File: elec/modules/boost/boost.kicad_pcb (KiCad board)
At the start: 2 copper layers, 40.6 x 61 mm, 9 parts, among them J1 Conn_01x05, J2 Conn_01x05, U1 LM2587S-ADJ

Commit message: sleepy but did most pcbs
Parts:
- added C35: 0.1uF, Capacitor_SMD:C_0603_1608Metric, F.Cu at (128.3, 102.9)
- added C36: 100uF, Capacitor_THT:CP_Radial_D8.0mm_P3.50mm, F.Cu at (130.0, 97.6)
- J1, J2: value Conn_01x05 -> Conn_01x08; footprint Pinheaders:PinHeader_1x05_P2.54mm_Vertical -> Pinheaders:PinHeader_1x08_P2.54mm_Vertical
- moved C40 36.5 mm to (149.0, 117.9), turned to 90 degrees
- moved R35 34.2 mm to (146.3, 116.9), turned to 180 degrees
- moved R38 33.9 mm to (146.3, 118.7), turned to 0 degrees
- moved J1 33.5 mm to (130.3, 91.1), turned to 90 degrees
- moved D2 32.3 mm to (149.8, 113.4), turned to 90 degrees
- moved R36 30.7 mm to (145.5, 114.4), turned to 90 degrees
- moved U1 24.6 mm to (131.5, 115.2), turned to 180 degrees
- moved J2 10.3 mm to (130.3, 123.4), turned to 90 degrees
- moved L33 9.96 mm to (138.0, 102.1), turned to 0 degrees
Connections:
- J1 pad 1: +24V -> +12V
- J1 pad 2: +24V -> +12V
- J1 pad 3: GND -> +12V
- J1 pad 4: +12V -> unconnected-(J1-Pin_4-Pad4)
- J1 pad 5: +12V -> unconnected-(J1-Pin_5-Pad5)
- J2 pad 1: +24V -> unconnected-(J2-Pin_1-Pad1)
- J2 pad 2: +24V -> unconnected-(J2-Pin_2-Pad2)
- J2 pad 3: GND -> +24V
- J2 pad 4: +12V -> +24V
- J2 pad 5: +12V -> +24V
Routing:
- net GND: vias 929 -> 2
- net +24V: vias 64 -> 0
- removed copper zone on B.Cu, net +24V
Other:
- board size 40.6 x 61 mm -> 30.5 x 40.6 mm

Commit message: finished pcbs-silkscrfeen pcbs seem halal
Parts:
- moved J1 2.49 mm to (130.3, 88.7)
- moved J2 0.20 mm to (130.3, 123.6)
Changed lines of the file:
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@@
 	(footprint "Pinheaders:PinHeader_1x08_P2.54mm_Vertical"
 		(layer "F.Cu")
-		(at 130.285 123.39 90)
+		(at 130.285 123.59 90)
 		(descr "Through hole straight pin header, 1x08, 2.54mm pitch, single row")
 		(tags "Through hole pin header THT 1x08 2.54mm single row")
@@
 	(footprint "Pinheaders:PinHeader_1x08_P2.54mm_Vertical"
 		(layer "F.Cu")
-		(at 130.285 91.14 90)
+		(at 130.285 88.65 90)
 		(descr "Through hole straight pin header, 1x08, 2.54mm pitch, single row")
 		(tags "Through hole pin header THT 1x08 2.54mm single row")
@@
 		(polygon
 			(pts
-				(xy 144.27 112.64) (xy 144.27 107.39) (xy 136.52 107.39) (xy 137.02 107.39) (xy 137.02 89.39) (xy 128.52 89.39)
+				(xy 144.27 112.64) (xy 144.27 107.39) (xy 136.52 107.39) (xy 137.02 107.39) (xy 137.02 87.14) (xy 128.52 87.14)
 				(xy 128.52 109.39) (xy 138.27 109.39) (xy 138.52 109.64) (xy 138.52 112.64)
 			)

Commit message: added silkscreen
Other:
- board text added: "design of 2-Chairs. 2025 JLC Order No. JLCJLCJLCJLC"
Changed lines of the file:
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@@
 		(layer "Edge.Cuts")
+	)
+	(gr_text "design of 2-Chairs. 2025\nJLC Order No. JLCJLCJLCJLC"
+		(at 138.77 103.14 0)
+		(layer "B.SilkS")
+		(effects
+			(font
+				(size 1 1)
+				(thickness 0.2)
+			)
+			(justify mirror)
+		)
 	)
 	(via

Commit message: did pcba for buck and boos5t
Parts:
- moved L33 6.56 mm to (144.3, 100.1)
- moved C35 5.27 mm to (132.8, 105.6)
- moved C36 4.51 mm to (134.4, 98.6)
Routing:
- net GND: vias 2 -> 3
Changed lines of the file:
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@@
 		(sheetname "/")
 		(sheetfile "boost.kicad_sch")
-		(attr through_hole)
+		(attr through_hole exclude_from_pos_files exclude_from_bom)
 		(fp_line
 			(start -1.33 -1.33)
@@
 		(sheetname "/")
 		(sheetfile "boost.kicad_sch")
-		(attr through_hole)
+		(attr through_hole exclude_from_pos_files exclude_from_bom)
 		(fp_line
 			(start 7.65 -3.26)
@@
 		(sheetname "/")
 		(sheetfile "boost.kicad_sch")
-		(attr through_hole)
+		(attr through_hole exclude_from_pos_files exclude_from_bom)
 		(fp_line
 			(start -1.33 -1.33)
@@
 	(footprint "Capacitor_THT:CP_Radial_D8.0mm_P3.50mm"
 		(layer "F.Cu")
-		(at 130.02 97.64 180)
+		(at 134.422651 98.64 180)
 		(descr "CP, Radial series, Radial, pin pitch=3.50mm, diameter=8mm, height=12mm, Electrolytic Capacitor")
 		(tags "CP Radial series Radial pin pitch 3.50mm diameter 8mm height 12mm Electrolytic Capacitor")
@@
 		(sheetname "/")
 		(sheetfile "boost.kicad_sch")
-		(attr through_hole)
+		(attr through_hole exclude_from_pos_files exclude_from_bom)
 		(fp_line
 			(start 5.83 -0.533)
@@
 	(footprint "Capacitor_SMD:C_0603_1608Metric"
 		(layer "F.Cu")
-		(at 128.27 102.89 180)
+		(at 132.77 105.64 180)
 		(descr "Capacitor SMD 0603 (1608 Metric), square (rectangular) end terminal, IPC-7351 nominal, (Body size source: IPC-SM-782 page 76, https://www.pcb-3d.com/wordpress/wp-content/uploads/ipc-sm-782a_amendment_1_and_2.pdf), generated with kicad-footprint-generator")
 		(tags "capacitor")
@@
 	(footprint "Inductor_SMD:L_APV_APH1040"
 		(layer "F.Cu")
-		(at 138.02 102.14)
+		(at 144.27 100.14)
 		(descr "Inductor, APV, APH1040, 10.8x10.0x3.8mm, (http://en.apvind.com/public/upload/20240408/996aafa961154ed753e4983e7eb80fa7.pdf), generated with kicad-footprint-generator gen_inductor.py")
 		(tags "molded power shielded")
@@
 		(net 2)
 	)
+	(via
+		(at 131.995 105.64)
+		(size 0.6)
+		(drill 0.3)
+		(layers "F.Cu" "B.Cu")
+		(net 2)
+	)
 	(zone
 		(net 5)
@@
 		(polygon
 			(pts
-				(xy 144.27 112.64) (xy 144.27 107.39) (xy 136.52 107.39) (xy 137.02 107.39) (xy 137.02 87.14) (xy 128.52 87.14)
-				(xy 128.52 109.39) (xy 138.27 109.39) (xy 138.52 109.64) (xy 138.52 112.64)
+				(xy 144.27 112.64) (xy 144.27 107.39) (xy 144.27 97.14) (xy 136.77 97.14) (xy 136.77 87.14) (xy 128.02 87.14)
+				(xy 128.02 109.39) (xy 138.27 109.39) (xy 138.52 109.64) (xy 138.52 112.64)
 			)
 		)
@@
 		(polygon
 			(pts
-				(xy 144.27 112.64) (xy 144.27 107.39) (xy 137.02 107.39) (xy 137.02 97.14) (xy 151.77 97.14) (xy 151.77 110.85)
-				(xy 146.52 110.85) (xy 146.52 112.89) (xy 144.77 112.89) (xy 144.77 114.64) (xy 140.02 114.64) (xy 140.02 112.64)
+				(xy 144.27 112.64) (xy 144.27 97.14) (xy 151.77 97.14) (xy 151.77 110.85) (xy 146.52 110.85) (xy 146.52 112.89)
+				(xy 144.77 112.89) (xy 144.77 114.64) (xy 140.02 114.64) (xy 140.02 112.64)
 			)
 		)

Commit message: added Bourns TC33X-2-104E
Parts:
- removed R35: 36.9K/56k, Capacitor_SMD:C_0603_1608Metric
- added VR1: TC33X-2-104E, Bourns TC33X-2-104E:TC33X2104E, F.Cu at (149.5, 114.6)
- moved D2 4.21 mm to (149.8, 109.2)
- moved L33 4.00 mm to (144.3, 96.1)
- moved U1 1.75 mm to (129.8, 115.2)
- moved R36 1.24 mm to (144.5, 115.1), turned to 180 degrees
- moved C36 1.00 mm to (134.4, 97.6)
- moved C40 0.74 mm to (149.3, 118.6), turned to 0 degrees
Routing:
- added copper zone on B.Cu, net +24V

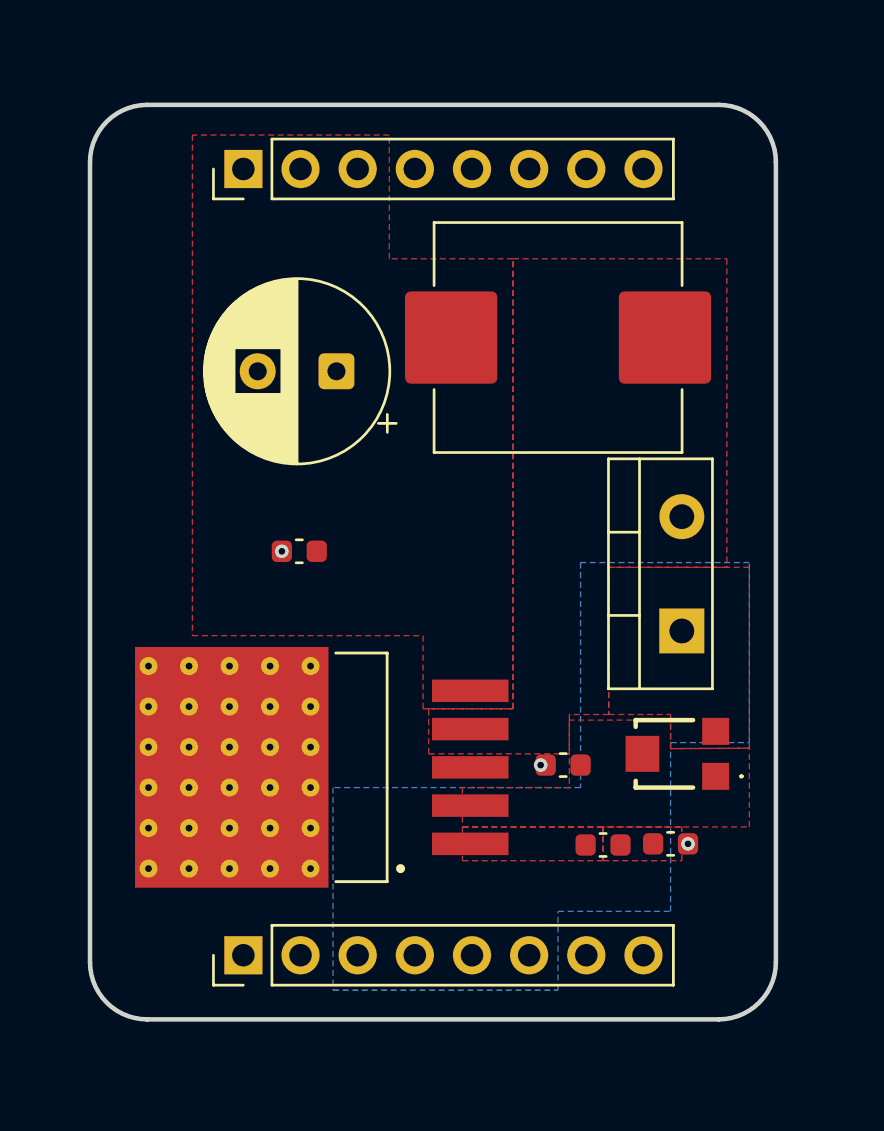
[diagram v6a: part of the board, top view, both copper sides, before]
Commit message: feat: added pot to boost
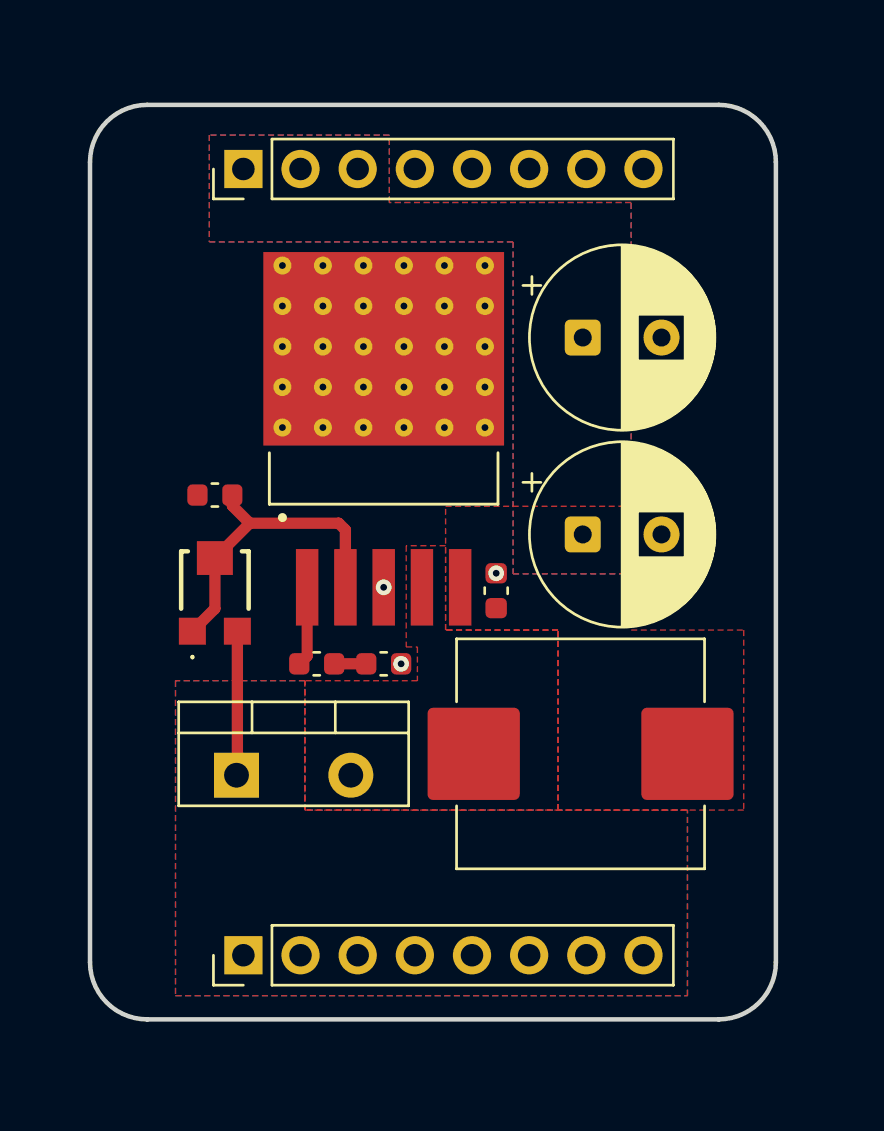
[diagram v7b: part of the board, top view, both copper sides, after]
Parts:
- added C1: 100uF, Capacitor_THT:CP_Radial_D8.0mm_P3.50mm, F.Cu at (145.4, 96.1)
- moved VR1 21.7 mm to (129.0, 107.4), turned to 0 degrees
- moved D2 20.8 mm to (130.0, 115.6), turned to 0 degrees
- moved U1 19.8 mm to (136.5, 96.6), turned to 90 degrees
- moved R36 19.6 mm to (129.0, 103.1)
- moved L33 18.5 mm to (145.3, 114.6), turned to 180 degrees
- moved R38 15.1 mm to (133.5, 110.6)
- moved C40 15.1 mm to (136.5, 110.6)
- moved C36 13.1 mm to (145.4, 104.9), turned to 0 degrees
- moved C35 8.92 mm to (141.5, 107.4), turned to 90 degrees
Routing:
- net Net-(U1-FB): track 0.00 -> 14.4 mm
- net +24V: track 0.00 -> 6.36 mm
- net Net-(U1-COMP): track 0.00 -> 3.54 mm
- net Net-(C40-Pad1): track 0.00 -> 1.43 mm
- added copper zone on B.Cu, net +12V
- removed copper zone on F.Cu, net Net-(C40-Pad1)
- removed copper zone on F.Cu, net Net-(U1-COMP)
- removed copper zone on F.Cu, net Net-(U1-FB)
